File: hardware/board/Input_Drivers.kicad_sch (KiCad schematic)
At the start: 14 parts

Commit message: Schematic getting closer to being finished
Schematic should be close to being ready to assign MPNs.
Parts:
- C? (x2): value 3.3n -> 1n
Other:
- note added: "Reduces Input Amplitude, Corrects Signal Inversion, and Limits High Frequencies into the Filter Core Input Amplitude ±5v Nominal Output Amplitude: ±50mV Nominal max Cutoff Frequency: ~80kHz"
- note removed: "Reduces Input Amplitude, Corrects Signal Inversion, and Limits High Frequencies into the Filter Core Input Amplitude ±5v Nominal Output Amplitude: ±50mV Nominal max Cutoff Frequency: ~20kHz"
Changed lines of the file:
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@@
     (effects (font (size 5 5) (thickness 0.508) bold) (justify left bottom))
   )
-  (text "Reduces Input Amplitude, Corrects Signal Inversion, and Limits High Frequencies into the Filter Core\n\nInput Amplitude\n±5v Nominal\n\nOutput Amplitude:\n±50mV Nominal max\n\nCutoff Frequency:\n~20kHz\n\n\n"
+  (text "Reduces Input Amplitude, Corrects Signal Inversion, and Limits High Frequencies into the Filter Core\n\nInput Amplitude\n±5v Nominal\n\nOutput Amplitude:\n±50mV Nominal max\n\nCutoff Frequency:\n~80kHz\n\n\n"
     (at 19.05 52.07 0)
     (effects (font (size 1.27 1.27)) (justify left bottom))
@@
       (effects (font (size 1.27 1.27)))
     )
-    (property "Value" "3.3n" (at 93.9736 80.01 90)
+    (property "Value" "1n" (at 93.9736 80.01 90)
       (effects (font (size 1.27 1.27)))
     )
@@
         )
         (path "/960bd036-bf0c-45ea-9f41-1321756e0e5a/3a92f97b-4bc8-4105-8c8c-23425d8f2338"
-          (reference "C4") (unit 1)
+          (reference "C?") (unit 1)
         )
       )
@@
       (effects (font (size 1.27 1.27)) (justify left))
     )
-    (property "Value" "3.3n" (at 198.12 113.6713 0)
+    (property "Value" "1n" (at 198.12 113.6713 0)
       (effects (font (size 1.27 1.27)) (justify left))
     )
@@
         )
         (path "/960bd036-bf0c-45ea-9f41-1321756e0e5a/3a92f97b-4bc8-4105-8c8c-23425d8f2338"
-          (reference "C5") (unit 1)
-        )
-      )
+          (reference "C?") (unit 1)
+        )
+      )

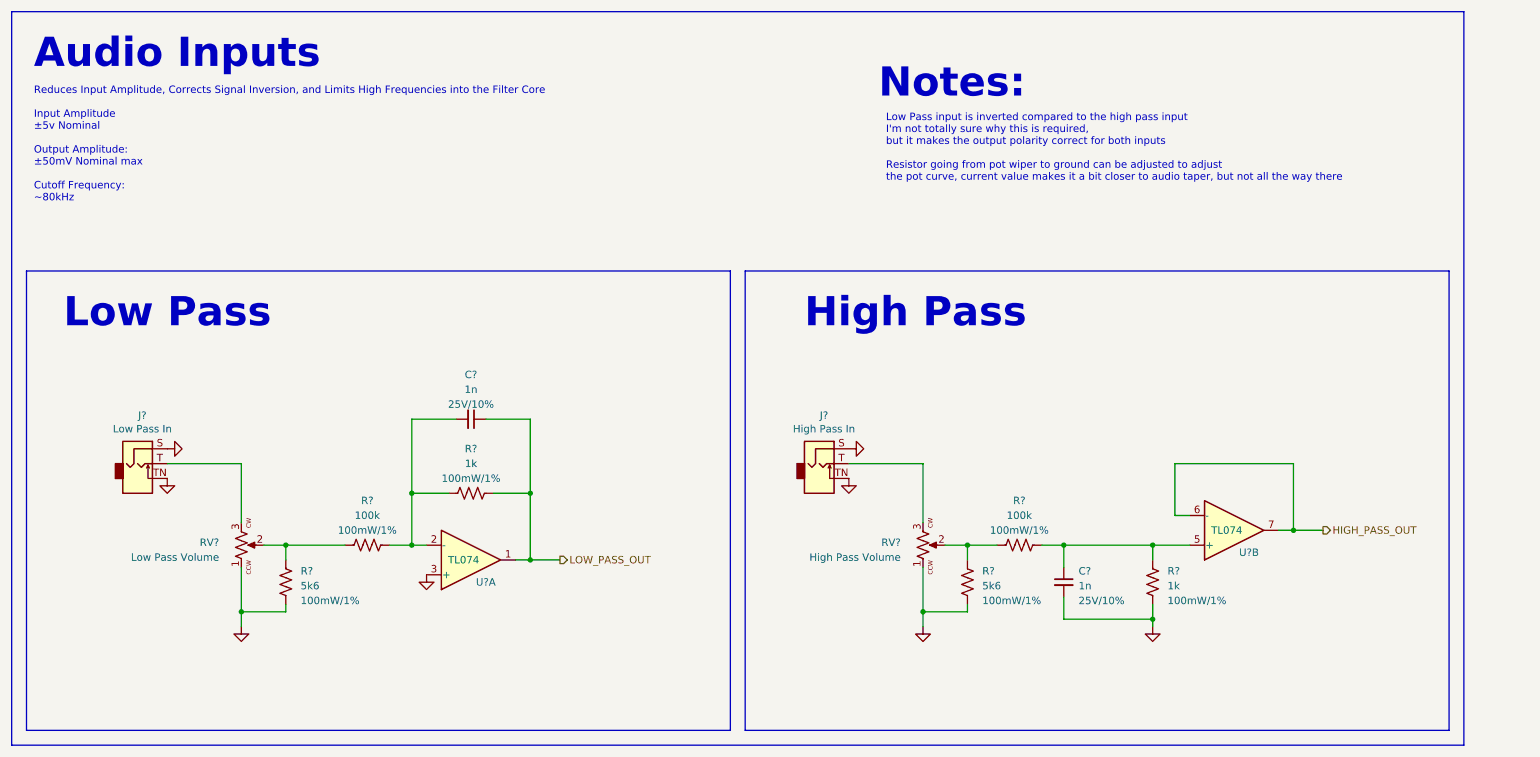
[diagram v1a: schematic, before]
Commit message: BOM Consolidation
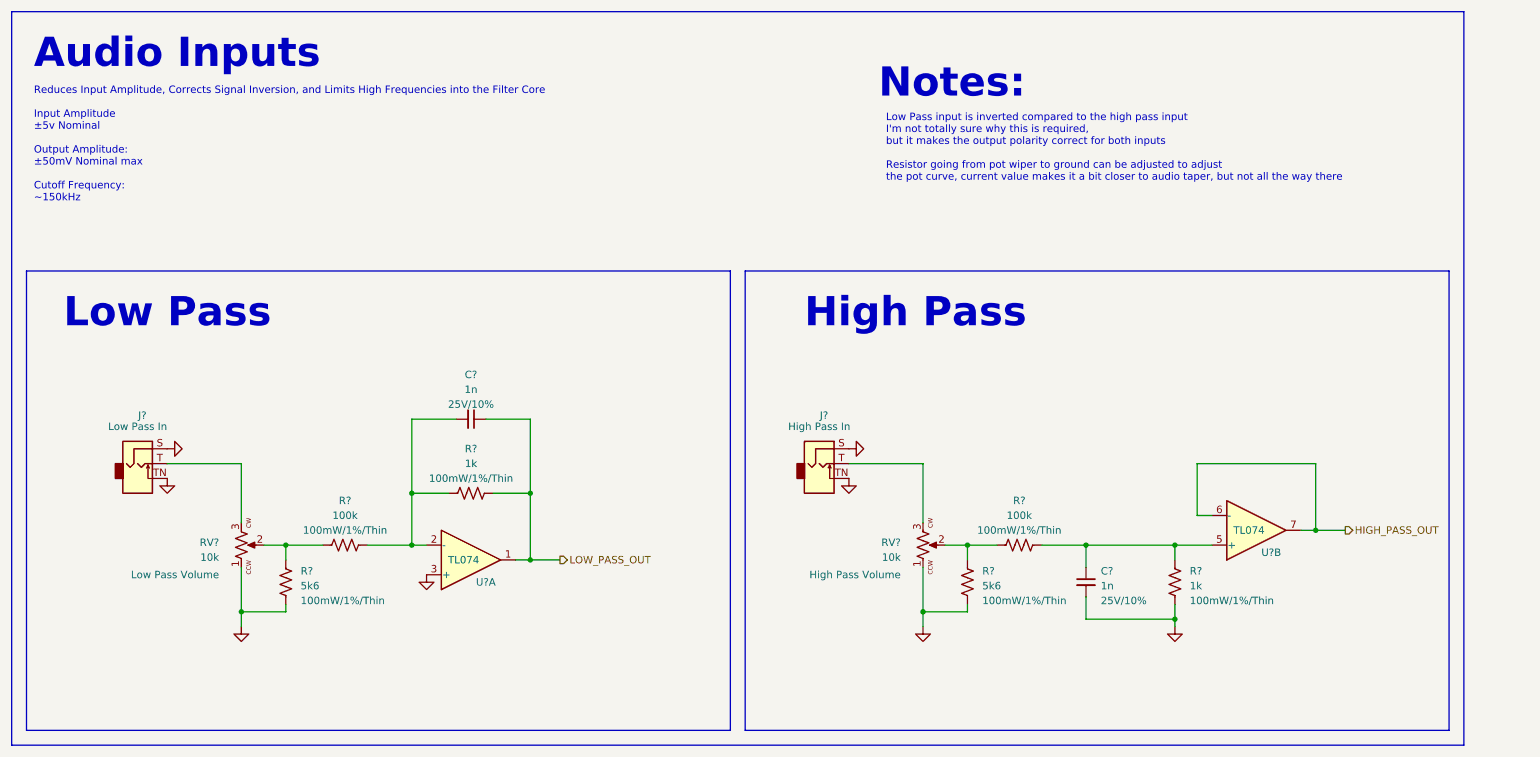
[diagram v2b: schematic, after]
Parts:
- J?: value High Pass In -> ~; Name (none) -> High Pass In
- J?: value Low Pass In -> ~; Name (none) -> Low Pass In
- R? (x6): Rating 100mW/1% -> 100mW/1%/Thin
- RV?: value High Pass Volume -> 10k; Name (none) -> High Pass Volume
- RV?: value Low Pass Volume -> 10k; Name (none) -> Low Pass Volume
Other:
- note added: "Reduces Input Amplitude, Corrects Signal Inversion, and Limits High Frequencies into the Filter Core Input Amplitude ±5v Nominal Output Amplitude: ±50mV Nominal max Cutoff Frequency: ~150kHz"
- note removed: "Reduces Input Amplitude, Corrects Signal Inversion, and Limits High Frequencies into the Filter Core Input Amplitude ±5v Nominal Output Amplitude: ±50mV Nominal max Cutoff Frequency: ~80kHz"
- moved on the sheet: C?, R?, U?B

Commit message: Updates for LED Drivers
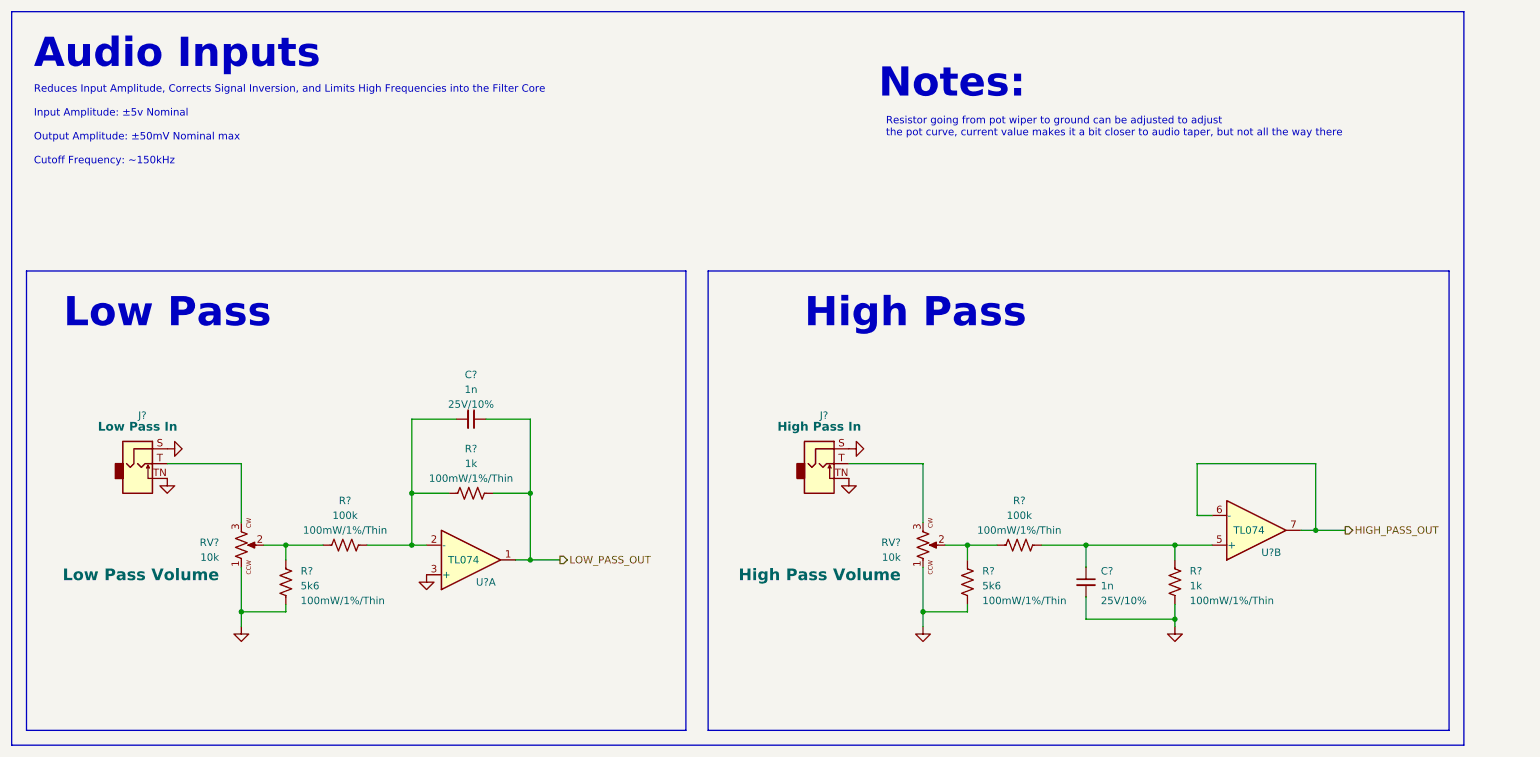
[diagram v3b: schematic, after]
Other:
- note added: "Reduces Input Amplitude, Corrects Signal Inversion, and Limits High Frequencies into the Filter Core Input Amplitude: ±5v Nominal Output Amplitude: ±50mV Nominal max Cutoff Frequency: ~150kHz"
- note added: "Resistor going from pot wiper to ground can be adjusted to adjust the pot curve, current value makes it a bit closer to audio taper, but not all the way there"
- note removed: "Low Pass input is inverted compared to the high pass input I'm not totally sure why this is required, but it makes the output polarity correct for both inputs Resistor going from pot wiper to ground can be adjusted to adjust the pot curve, current value makes it a bit closer to audio taper, but not all the way there"
- note removed: "Reduces Input Amplitude, Corrects Signal Inversion, and Limits High Frequencies into the Filter Core Input Amplitude ±5v Nominal Output Amplitude: ±50mV Nominal max Cutoff Frequency: ~150kHz"
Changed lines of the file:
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@@
     (fill (type none))
   )
-  (rectangle (start 17.78 59.69) (end 138.43 138.43)
+  (rectangle (start 17.78 59.69) (end 130.81 138.43)
     (stroke (width 0) (type default))
     (fill (type none))
   )
-  (rectangle (start 140.97 59.69) (end 261.62 138.43)
+  (rectangle (start 134.62 59.69) (end 261.62 138.43)
     (stroke (width 0) (type default))
     (fill (type none))
   )
-  (text "Low Pass input is inverted compared to the high pass input\nI'm not totally sure why this is required,\nbut it makes the output polarity correct for both inputs\n\nResistor going from pot wiper to ground can be adjusted to adjust\nthe pot curve, current value makes it a bit closer to audio taper, but not all the way there"
-    (at 165.1 44.45 0)
+  (text "Resistor going from pot wiper to ground can be adjusted to adjust\nthe pot curve, current value makes it a bit closer to audio taper, but not all the way there"
+    (at 165.1 36.83 0)
     (effects (font (size 1.27 1.27)) (justify left bottom))
   )
@@
     (effects (font (size 5 5) (thickness 0.508) bold) (justify left bottom))
   )
-  (text "Reduces Input Amplitude, Corrects Signal Inversion, and Limits High Frequencies into the Filter Core\n\nInput Amplitude\n±5v Nominal\n\nOutput Amplitude:\n±50mV Nominal max\n\nCutoff Frequency:\n~150kHz\n\n\n"
-    (at 19.05 52.07 0)
+  (text "Reduces Input Amplitude, Corrects Signal Inversion, and Limits High Frequencies into the Filter Core\n\nInput Amplitude: ±5v Nominal\n\nOutput Amplitude: ±50mV Nominal max\n\nCutoff Frequency: ~150kHz\n\n\n"
+    (at 19.05 45.72 0)
     (effects (font (size 1.27 1.27)) (justify left bottom))
   )
@@
     )
     (property "Name" "High Pass Volume" (at 167.64 111.76 90)
-      (effects (font (size 1.27 1.27)) (justify left))
+      (effects (font (size 2 2) bold) (justify left))
     )
     (pin "1")
@@
     )
     (property "Name" "High Pass In" (at 153.67 86.36 0)
-      (effects (font (size 1.27 1.27)))
+      (effects (font (size 1.5 1.5) bold))
     )
     (pin "S")
@@
     )
     (property "Name" "Low Pass Volume" (at 50.8 111.76 90)
-      (effects (font (size 1.27 1.27)) (justify left))
+      (effects (font (size 2 2) bold) (justify left))
     )
     (pin "1")
@@
     )
     (property "Name" "Low Pass In" (at 36.83 86.36 0)
-      (effects (font (size 1.27 1.27)))
+      (effects (font (size 1.5 1.5) bold))
     )
     (pin "S")

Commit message: hardware: update schematic with footprints and preliminary MPNs
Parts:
- C? (x2), R? (x6): smd kit 1 -> (none)
- J? (x2): mpn WQP-WQP518MA -> (none)
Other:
- title: Diode Ladder Filter -> Neptune

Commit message: Very first component layout.
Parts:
- removed U? (x2): TL074, Package_SO:TSSOP-14_4.4x5mm_P0.65mm, symbol winterbloom:TL074
- added U? (x2): TL074, Package_SO:TSSOP-14_4.4x5mm_P0.65mm, symbol winterbloom:TL074
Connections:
- net GND: now also U?.3 (+)
- net HIGH_PASS_OUT: now also U?.6 (-), U?.7
- net LOW_PASS_OUT: now also U?.1
- net at C?.2, R?.1, R?.2: now also U?.2 (-)
- net at C?.1, R?.1, R?.1: now also U?.5 (+)

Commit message: Rough Draft of Routing Complete. Ugly but Passes DRC
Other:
- note added: "Resistor going from pot wiper to ground can be adjusted to adjust the volume curve"
- note removed: "Resistor going from pot wiper to ground can be adjusted to adjust the pot curve, current value makes it a bit closer to audio taper, but not all the way there"
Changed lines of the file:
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@@
     (fill (type none))
   )
-  (text "Resistor going from pot wiper to ground can be adjusted to adjust\nthe pot curve, current value makes it a bit closer to audio taper, but not all the way there"
-    (at 19.05 55.88 0)
+  (text "Resistor going from pot wiper to ground can be adjusted to adjust the volume curve"
+    (at 19.05 52.705 0)
     (effects (font (size 1.27 1.27)) (justify left bottom))
   )

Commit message: hardware: minor fixes and aesthetic updates
- Fix HP LEDs being backwards
- Switch power header, pot, and jack footprints to longpad variants
- Make the text size on the front side larger
- Add "red" and "blue" text next to respective LEDs on front side
- Adjusted zone thermal spoke for better connection to GND pads
- Squished the solder jumpers for instability type closer together
- Minor adjustments to traces to accommodate longpad footprints
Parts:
- J? (x2): footprint winterbloom:AudioJack_WQP518MA_Compact_S -> winterbloom:AudioJack_WQP518MA_Compact_S_LongPads
- RV? (x2): footprint winterbloom:Potentiometer_Alpha_R0904N -> winterbloom:Potentiometer_Alpha_R0904N_LongPads
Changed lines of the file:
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@@
       (effects (font (size 1.27 1.27)) (justify left))
     )
-    (property "Footprint" "winterbloom:Potentiometer_Alpha_R0904N" (at 182.88 106.68 0)
+    (property "Footprint" "winterbloom:Potentiometer_Alpha_R0904N_LongPads" (at 182.88 106.68 0)
       (effects (font (size 1.27 1.27)) hide)
     )
@@
       (effects (font (size 1.27 1.27)))
     )
-    (property "Footprint" "winterbloom:AudioJack_WQP518MA_Compact_S" (at 152.4 85.09 0)
+    (property "Footprint" "winterbloom:AudioJack_WQP518MA_Compact_S_LongPads" (at 152.4 85.09 0)
       (effects (font (size 1.27 1.27)) hide)
     )
@@
       (effects (font (size 1.27 1.27)) (justify left))
     )
-    (property "Footprint" "winterbloom:Potentiometer_Alpha_R0904N" (at 66.04 106.68 0)
+    (property "Footprint" "winterbloom:Potentiometer_Alpha_R0904N_LongPads" (at 66.04 106.68 0)
       (effects (font (size 1.27 1.27)) hide)
     )
@@
       (effects (font (size 1.27 1.27)))
     )
-    (property "Footprint" "winterbloom:AudioJack_WQP518MA_Compact_S" (at 35.56 85.09 0)
-      (effects (font (size 1.27 1.27)) hide)
-    )
+    (property "Footprint" "winterbloom:AudioJack_WQP518MA_Compact_S_LongPads" (at 35.56 85.09 0)
+      (effects (font (size 1.27 1.27)) hide)
+    )
